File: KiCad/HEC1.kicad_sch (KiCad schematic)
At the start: 36 parts, among them J1 Barrel_Jack_Switch, U35 74LS08, U41 74LS02

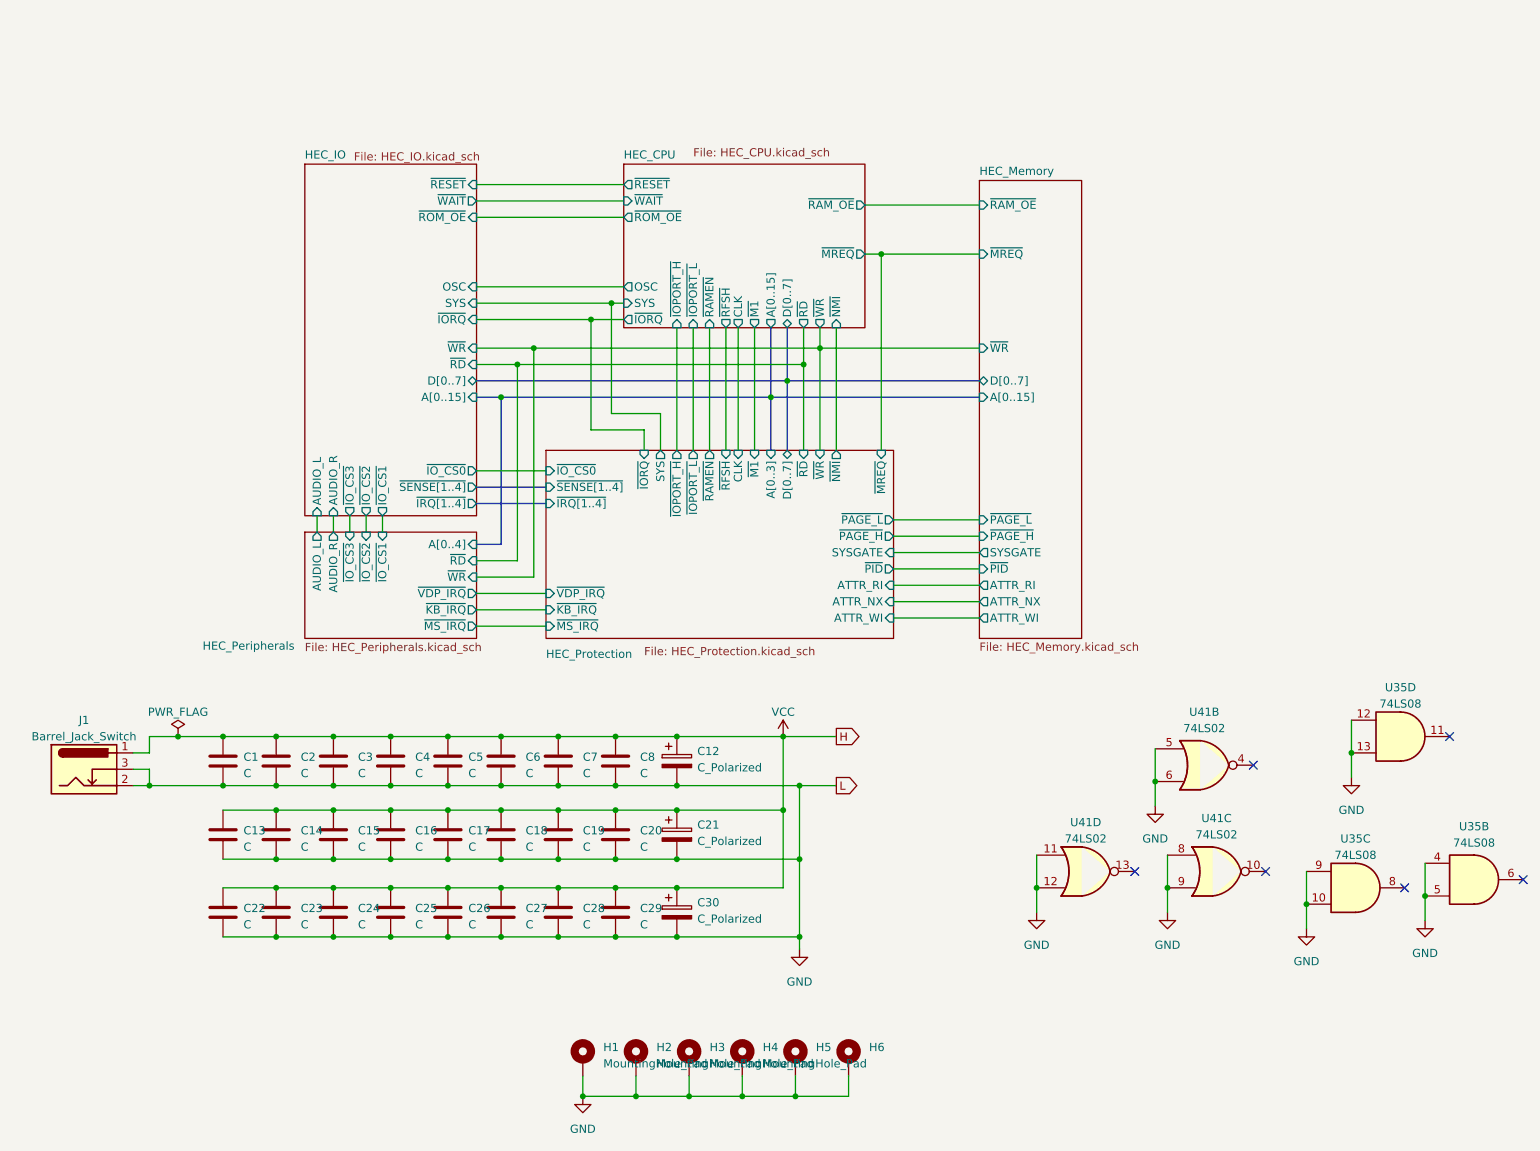
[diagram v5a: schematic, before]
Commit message: Preliminary layout
Very early stage layout prototype, very subject to change.
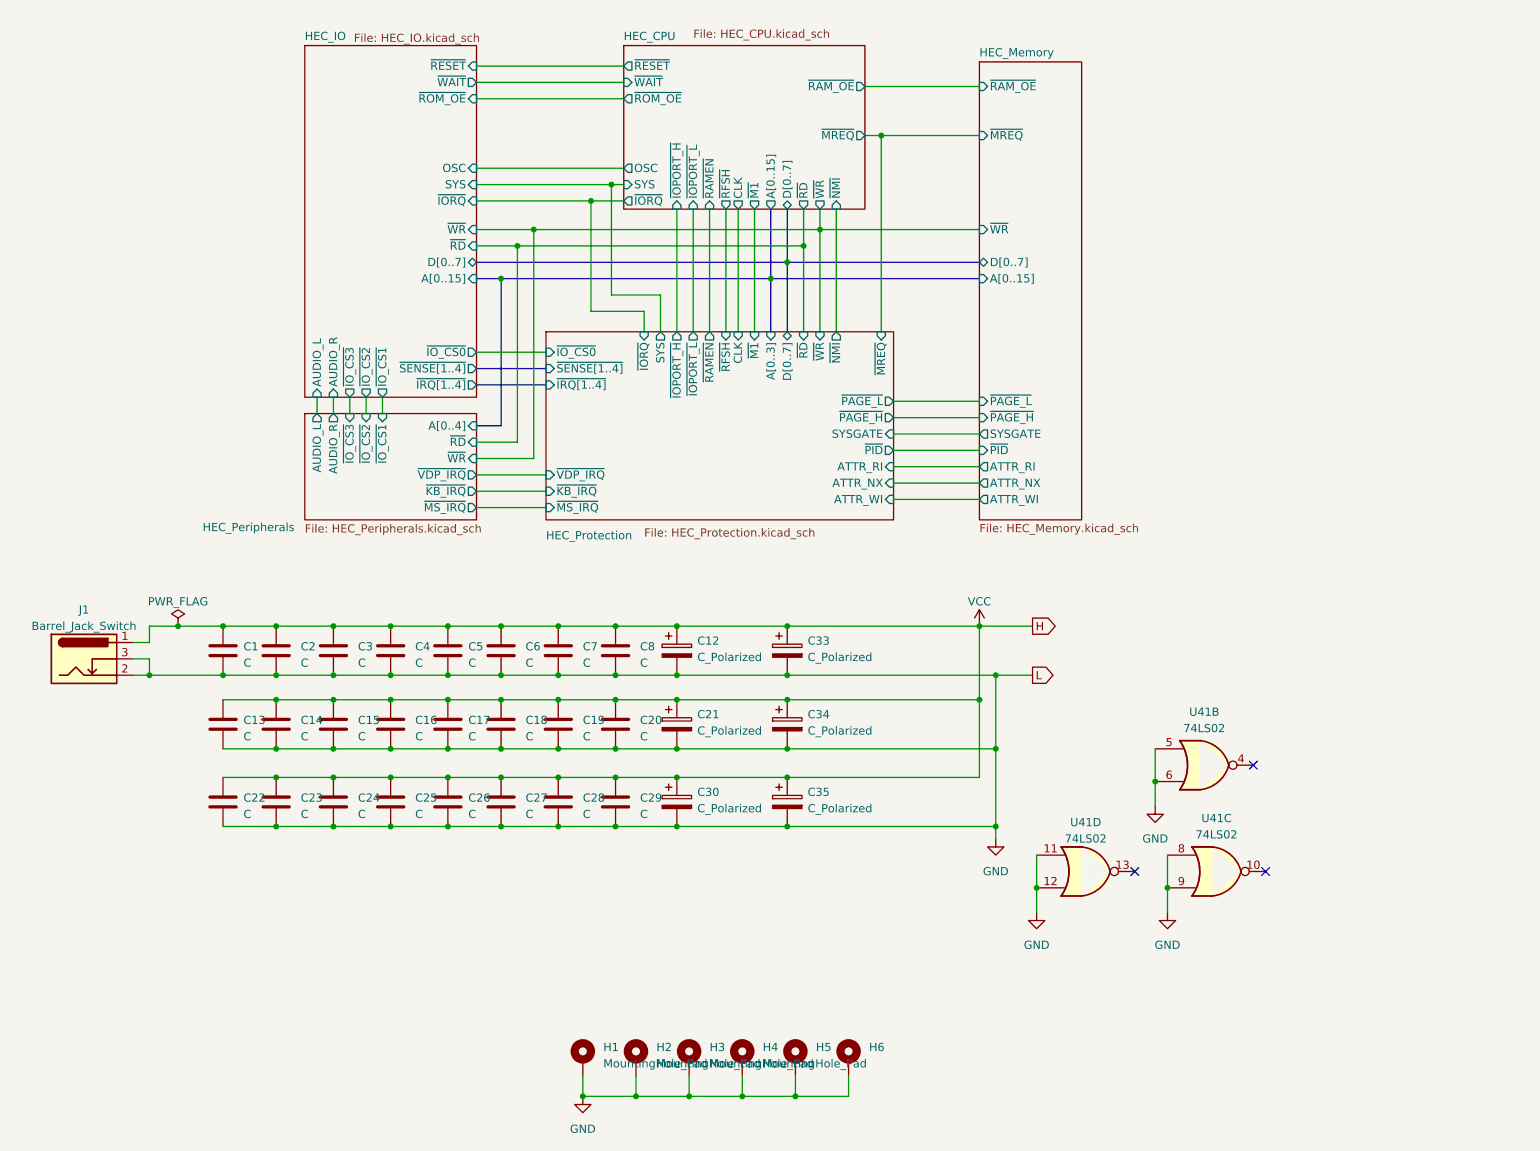
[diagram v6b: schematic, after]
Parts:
- removed U35: 74LS08, Package_DIP:DIP-14_W7.62mm_Socket, symbol 74xx:74LS08
- added C33, C34, C35: C_Polarized, Capacitor_THT:CP_Radial_D10.0mm_P5.00mm, symbol Device:C_Polarized
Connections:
- net GND: now also C33.2, C34.2, C35.2
- net VCC: now also C33.1, C34.1, C35.1
- no-connect marks 6 -> 3
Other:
- moved on the sheet: C1, C12, C13, C14, C15, C16, C17, C18, C19, C2, C20, C21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

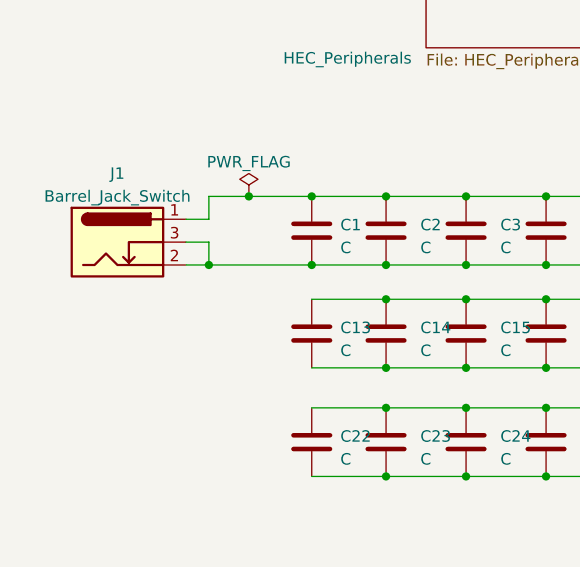
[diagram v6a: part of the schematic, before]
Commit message: Updated layout
Updated the layout of PCB. Chips on the board in this version might be in their final position.
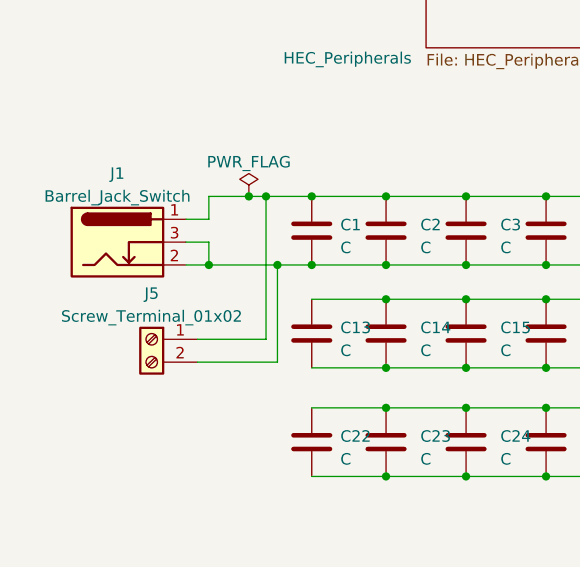
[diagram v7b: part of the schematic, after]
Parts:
- added J5: Screw_Terminal_01x02, TerminalBlock_MetzConnect:TerminalBlock_MetzConnect_Type073_RT02602HBLU_1x02_P5.08mm_Horizontal, symbol Connector:Screw_Terminal_01x02
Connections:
- net GND: now also J5.2 (Pin_2)
- net VCC: now also J5.1 (Pin_1)
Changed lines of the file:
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@@
   (junction (at 108.585 135.89) (diameter 0) (color 0 0 0 0)
   )
+  (junction (at 69.85 120.015) (diameter 0) (color 0 0 0 0)
+  )
   (junction (at 125.73 120.015) (diameter 0) (color 0 0 0 0)
   )
@@
   )
   (junction (at 119.38 53.34) (diameter 0) (color 0 0 0 0)
+  )
+  (junction (at 68.58 112.395) (diameter 0) (color 0 0 0 0)
   )
   (junction (at 66.675 112.395) (diameter 0) (color 0 0 0 0)
@@
     (stroke (width 0) (type default))
   )
+  (wire (pts (xy 60.96 128.27) (xy 68.58 128.27))
+    (stroke (width 0) (type default))
+  )
   (wire (pts (xy 113.03 30.48) (xy 135.89 30.48))
     (stroke (width 0) (type default))
@@
     (stroke (width 0) (type default))
   )
-  (wire (pts (xy 66.675 112.395) (xy 73.66 112.395))
+  (wire (pts (xy 66.675 112.395) (xy 68.58 112.395))
     (stroke (width 0) (type default))
   )
@@
     (stroke (width 0) (type default))
   )
+  (wire (pts (xy 69.85 120.015) (xy 73.66 120.015))
+    (stroke (width 0) (type default))
+  )
   (wire (pts (xy 59.69 120.015) (xy 62.23 120.015))
     (stroke (width 0) (type default))
@@
     (stroke (width 0) (type default))
   )
+  (wire (pts (xy 68.58 112.395) (xy 73.66 112.395))
+    (stroke (width 0) (type default))
+  )
   (wire (pts (xy 95.885 76.835) (xy 95.885 79.375))
     (stroke (width 0) (type default))
@@
     (stroke (width 0) (type default))
   )
-  (wire (pts (xy 62.23 120.015) (xy 73.66 120.015))
+  (wire (pts (xy 62.23 120.015) (xy 69.85 120.015))
     (stroke (width 0) (type default))
   )
@@
     (stroke (width 0) (type default))
   )
+  (wire (pts (xy 60.96 130.81) (xy 69.85 130.81))
+    (stroke (width 0) (type default))
+  )
   (wire (pts (xy 125.73 143.51) (xy 134.62 143.51))
     (stroke (width 0) (type default))
@@
     (stroke (width 0) (type default))
   )
+  (wire (pts (xy 69.85 130.81) (xy 69.85 120.015))
+    (stroke (width 0) (type default))
+  )
   (wire (pts (xy 62.23 117.475) (xy 62.23 120.015))
     (stroke (width 0) (type default))
@@
   )
   (wire (pts (xy 81.915 112.395) (xy 90.805 112.395))
+    (stroke (width 0) (type default))
+  )
+  (wire (pts (xy 68.58 128.27) (xy 68.58 112.395))
     (stroke (width 0) (type default))
   )
@@
         )
       )
+    )
+  )
+  (symbol (lib_id "Connector:Screw_Terminal_01x02") (at 55.88 128.27 0) (mirror y) (unit 1)
+    (in_bom yes) (on_board yes) (dnp no) (fields_autoplaced)
+    (property "Reference" "J5" (at 55.88 123.19 0)
+      (effects (font (size 1.27 1.27)))
+    )
+    (property "Value" "Screw_Terminal_01x02" (at 55.88 125.73 0)
+      (effects (font (size 1.27 1.27)))
+    )
+    (property "Footprint" "TerminalBlock_MetzConnect:TerminalBlock_MetzConnect_Type073_RT02602HBLU_1x02_P5.08mm_Horizontal" (at 55.88 128.27 0)
+      (effects (font (size 1.27 1.27)) hide)
+    )
+    (property "Datasheet" "~" (at 55.88 128.27 0)
+      (effects (font (size 1.27 1.27)) hide)
+    )
+    (pin "1")
+    (pin "2")
+    (instances
+      (project "HEC1"
+        (path "/87935374-b60a-4f41-99da-94b76103dd77"
+          (reference "J5") (unit 1)
+        )
+      )

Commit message: Bug fixes
fixed some bugs introduced to the schematic. More routing.
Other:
- sheet HEC_IO ports: added ~{RAM_OE}; removed ~{RD}
- sheet HEC_Peripherals ports: added D[0..7], ~{RESET}; removed none
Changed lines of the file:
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@@
   (junction (at 162.56 185.42) (diameter 0) (color 0 0 0 0)
   )
+  (junction (at 118.11 55.88) (diameter 0) (color 0 0 0 0)
+  )
   (junction (at 90.805 143.51) (diameter 0) (color 0 0 0 0)
   )
@@
   (junction (at 175.895 36.195) (diameter 0) (color 0 0 0 0)
   )
-  (junction (at 119.38 53.34) (diameter 0) (color 0 0 0 0)
+  (junction (at 177.165 28.575) (diameter 0) (color 0 0 0 0)
   )
   (junction (at 68.58 112.395) (diameter 0) (color 0 0 0 0)
@@
   )
   (junction (at 116.84 131.445) (diameter 0) (color 0 0 0 0)
+  )
+  (junction (at 114.935 25.4) (diameter 0) (color 0 0 0 0)
   )
   (junction (at 191.135 123.825) (diameter 0) (color 0 0 0 0)
@@
     (stroke (width 0) (type default))
   )
+  (wire (pts (xy 117.475 33.02) (xy 113.03 33.02))
+    (stroke (width 0) (type default))
+  )
   (wire (pts (xy 108.585 120.015) (xy 116.84 120.015))
     (stroke (width 0) (type default))
@@
     (stroke (width 0) (type default))
   )
+  (wire (pts (xy 114.935 25.4) (xy 135.89 25.4))
+    (stroke (width 0) (type default))
+  )
   (wire (pts (xy 156.21 47.625) (xy 156.21 66.675))
     (stroke (width 0) (type default))
@@
     (stroke (width 0) (type default))
   )
-  (wire (pts (xy 113.03 88.9) (xy 123.825 88.9))
+  (wire (pts (xy 113.03 93.98) (xy 123.825 93.98))
     (stroke (width 0) (type default))
   )
@@
     (stroke (width 0) (type default))
   )
-  (wire (pts (xy 113.03 25.4) (xy 135.89 25.4))
+  (wire (pts (xy 113.03 25.4) (xy 114.935 25.4))
+    (stroke (width 0) (type default))
+  )
+  (wire (pts (xy 177.165 28.575) (xy 191.135 28.575))
     (stroke (width 0) (type default))
   )
@@
     (stroke (width 0) (type default))
   )
-  (bus (pts (xy 113.03 81.28) (xy 116.84 81.28))
-    (stroke (width 0) (type default))
-  )
-  (wire (pts (xy 113.03 83.82) (xy 119.38 83.82))
+  (bus (pts (xy 113.03 85.725) (xy 116.84 85.725))
+    (stroke (width 0) (type default))
+  )
+  (wire (pts (xy 113.03 88.9) (xy 119.38 88.9))
     (stroke (width 0) (type default))
   )
@@
     (stroke (width 0) (type default))
   )
-  (wire (pts (xy 113.03 93.98) (xy 123.825 93.98))
+  (wire (pts (xy 113.03 99.06) (xy 123.825 99.06))
     (stroke (width 0) (type default))
   )
@@
     (stroke (width 0) (type default))
   )
+  (wire (pts (xy 114.935 25.4) (xy 114.935 81.28))
+    (stroke (width 0) (type default))
+  )
+  (wire (pts (xy 177.165 17.145) (xy 117.475 17.145))
+    (stroke (width 0) (type default))
+  )
   (wire (pts (xy 163.83 47.625) (xy 163.83 53.34))
     (stroke (width 0) (type default))
@@
     (stroke (width 0) (type default))
   )
-  (bus (pts (xy 113.03 55.88) (xy 161.29 55.88))
+  (bus (pts (xy 113.03 55.88) (xy 118.11 55.88))
     (stroke (width 0) (type default))
   )
@@
     (stroke (width 0) (type default))
   )
-  (wire (pts (xy 173.355 28.575) (xy 191.135 28.575))
+  (wire (pts (xy 173.355 28.575) (xy 177.165 28.575))
     (stroke (width 0) (type default))
   )
@@
     (stroke (width 0) (type default))
   )
+  (wire (pts (xy 177.165 28.575) (xy 177.165 17.145))
+    (stroke (width 0) (type default))
+  )
   (wire (pts (xy 161.29 131.445) (xy 193.675 131.445))
     (stroke (width 0) (type default))
@@
     (stroke (width 0) (type default))
   )
+  (bus (pts (xy 118.11 55.88) (xy 161.29 55.88))
+    (stroke (width 0) (type default))
+  )
   (wire (pts (xy 191.135 112.395) (xy 191.135 123.825))
     (stroke (width 0) (type default))
   )
-  (wire (pts (xy 113.03 53.34) (xy 119.38 53.34))
-    (stroke (width 0) (type default))
-  )
   (wire (pts (xy 90.805 120.015) (xy 99.695 120.015))
     (stroke (width 0) (type default))
@@
     (stroke (width 0) (type default))
   )
-  (wire (pts (xy 121.92 86.36) (xy 121.92 50.8))
+  (wire (pts (xy 121.92 91.44) (xy 121.92 50.8))
     (stroke (width 0) (type default))
   )
@@
     (stroke (width 0) (type default))
   )
+  (bus (pts (xy 118.11 83.185) (xy 118.11 55.88))
+    (stroke (width 0) (type default))
+  )
   (wire (pts (xy 175.895 36.195) (xy 175.895 66.675))
     (stroke (width 0) (type default))
@@
     (stroke (width 0) (type default))
   )
+  (wire (pts (xy 117.475 17.145) (xy 117.475 33.02))
+    (stroke (width 0) (type default))
+  )
   (wire (pts (xy 99.695 131.445) (xy 108.585 131.445))
     (stroke (width 0) (type default))
@@
     (stroke (width 0) (type default))
   )
-  (wire (pts (xy 113.03 91.44) (xy 123.825 91.44))
+  (wire (pts (xy 113.03 96.52) (xy 123.825 96.52))
     (stroke (width 0) (type default))
   )
@@
     (stroke (width 0) (type default))
   )
-  (wire (pts (xy 119.38 83.82) (xy 119.38 53.34))
+  (wire (pts (xy 119.38 88.9) (xy 119.38 53.34))
     (stroke (width 0) (type default))
   )
@@
     (stroke (width 0) (type default))
   )
-  (bus (pts (xy 116.84 81.28) (xy 116.84 58.42))
+  (bus (pts (xy 116.84 85.725) (xy 116.84 58.42))
     (stroke (width 0) (type default))
   )
@@
     (stroke (width 0) (type default))
   )
+  (wire (pts (xy 114.935 81.28) (xy 113.03 81.28))
+    (stroke (width 0) (type default))
+  )
   (wire (pts (xy 116.84 135.89) (xy 125.73 135.89))
     (stroke (width 0) (type default))
@@
     (stroke (width 0) (type default))
   )
+  (bus (pts (xy 113.03 83.185) (xy 118.11 83.185))
+    (stroke (width 0) (type default))
+  )
   (wire (pts (xy 154.305 185.42) (xy 162.56 185.42))
     (stroke (width 0) (type default))
   )
-  (wire (pts (xy 113.03 86.36) (xy 121.92 86.36))
+  (wire (pts (xy 113.03 91.44) (xy 121.92 91.44))
     (stroke (width 0) (type default))
   )
@@
     )
   )
-  (sheet (at 123.825 66.675) (size 53.975 29.21)
+  (sheet (at 123.825 66.675) (size 53.975 34.29)
     (stroke (width 0.1524) (type solid))
     (fill (color 0 0 0 0.0000))
-    (property "Sheetname" "HEC_Protection" (at 123.825 99.06 0)
+    (property "Sheetname" "HEC_Protection" (at 123.825 104.14 0)
       (effects (font (size 1.27 1.27)) (justify left bottom))
     )
-    (property "Sheetfile" "HEC_Protection.kicad_sch" (at 139.065 97.155 0)
+    (property "Sheetfile" "HEC_Protection.kicad_sch" (at 139.065 102.235 0)
       (effects (font (size 1.27 1.27)) (justify left top))
     )
@@
       (effects (font (size 1.27 1.27)) (justify right))
     )
-    (pin "~{VDP_IRQ}" input (at 123.825 88.9 180)
-      (effects (font (size 1.27 1.27)) (justify left))
-    )
-    (pin "~{KB_IRQ}" input (at 123.825 91.44 180)
-      (effects (font (size 1.27 1.27)) (justify left))
-    )
-    (pin "~{MS_IRQ}" input (at 123.825 93.98 180)
+    (pin "~{VDP_IRQ}" input (at 123.825 93.98 180)
+      (effects (font (size 1.27 1.27)) (justify left))
+    )
+    (pin "~{KB_IRQ}" input (at 123.825 96.52 180)
+      (effects (font (size 1.27 1.27)) (justify left))
+    )
+    (pin "~{MS_IRQ}" input (at 123.825 99.06 180)
       (effects (font (size 1.27 1.27)) (justify left))
     )
@@
       (effects (font (size 1.27 1.27)) (justify left top))
     )
-    (pin "~{RD}" input (at 113.03 53.34 0)
-      (effects (font (size 1.27 1.27)) (justify right))
-    )
     (pin "A[0..15]" input (at 113.03 58.42 0)
       (effects (font (size 1.27 1.27)) (justify right))
@@
     (pin "AUDIO_L" input (at 88.265 76.835 270)
       (effects (font (size 1.27 1.27)) (justify left))
+    )
+    (pin "~{RAM_OE}" input (at 113.03 33.02 0)
+      (effects (font (size 1.27 1.27)) (justify right))
     )
     (instances
@@
     )
   )
-  (sheet (at 86.36 79.375) (size 26.67 16.51)
+  (sheet (at 86.36 79.375) (size 26.67 21.59)
     (stroke (width 0.1524) (type solid))
     (fill (color 0 0 0 0.0000))
-    (property "Sheetname" "HEC_Peripherals" (at 70.485 97.79 0)
+    (property "Sheetname" "HEC_Peripherals" (at 70.485 102.87 0)
       (effects (font (size 1.27 1.27)) (justify left bottom))
     )
-    (property "Sheetfile" "HEC_Peripherals.kicad_sch" (at 86.36 96.52 0)
+    (property "Sheetfile" "HEC_Peripherals.kicad_sch" (at 86.36 101.6 0)
       (effects (font (size 1.27 1.27)) (justify left top))
     )
-    (pin "~{VDP_IRQ}" output (at 113.03 88.9 0)
-      (effects (font (size 1.27 1.27)) (justify right))
-    )
-    (pin "~{KB_IRQ}" output (at 113.03 91.44 0)
-      (effects (font (size 1.27 1.27)) (justify right))
-    )
-    (pin "~{MS_IRQ}" output (at 113.03 93.98 0)
-      (effects (font (size 1.27 1.27)) (justify right))
-    )
-    (pin "~{RD}" input (at 113.03 83.82 0)
-      (effects (font (size 1.27 1.27)) (justify right))
-    )
-    (pin "~{WR}" input (at 113.03 86.36 0)
+    (pin "~{VDP_IRQ}" output (at 113.03 93.98 0)
+      (effects (font (size 1.27 1.27)) (justify right))
+    )
+    (pin "~{KB_IRQ}" output (at 113.03 96.52 0)
+      (effects (font (size 1.27 1.27)) (justify right))
+    )
+    (pin "~{MS_IRQ}" output (at 113.03 99.06 0)
+      (effects (font (size 1.27 1.27)) (justify right))
+    )
+    (pin "~{RD}" input (at 113.03 88.9 0)
+      (effects (font (size 1.27 1.27)) (justify right))
+    )
+    (pin "~{WR}" input (at 113.03 91.44 0)
       (effects (font (size 1.27 1.27)) (justify right))
     )
@@
       (effects (font (size 1.27 1.27)) (justify right))
     )
-    (pin "A[0..4]" input (at 113.03 81.28 0)
+    (pin "A[0..4]" input (at 113.03 85.725 0)
       (effects (font (size 1.27 1.27)) (justify right))
     )
@@
       (effects (font (size 1.27 1.27)) (justify right))
     )
+    (pin "~{RESET}" input (at 113.03 81.28 0)
+      (effects (font (size 1.27 1.27)) (justify right))
+    )
+    (pin "D[0..7]" input (at 113.03 83.185 0)
+      (effects (font (size 1.27 1.27)) (justify right))
+    )
